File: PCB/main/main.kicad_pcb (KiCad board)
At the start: 2 copper layers, 82.3 x 36.1 mm, 38 parts, among them IC1 LT8316IFE#PBF, Q1 PBHV9050ZF, Q2 IXTA10P50P, Q3 SIHB24N80AE-GE3, T1 Transformer_1P_2S

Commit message: pcb drawing update
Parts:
- C5: moved to B.Cu
- R11: footprint Resistor_SMD:R_0805_2012Metric -> Resistor_SMD:R_1218_3246Metric_Pad1.22x4.75mm_HandSolder; moved to B.Cu
- moved R11 16.4 mm to (101.1, 42.4), turned to 90 degrees
- moved R1 13.5 mm to (87.8, 47.9), turned to 270 degrees
- moved R7 12.2 mm to (92.2, 36.7), turned to 90 degrees
- moved R6 11.3 mm to (87.6, 36.3), turned to 90 degrees
- moved Vin1 10.9 mm to (82.3, 35.3)
- moved R10 10.8 mm to (97.8, 42.8)
- moved D2 10.6 mm to (89.9, 36.2), turned to 270 degrees
- moved REF** 9.63 mm to (79.6, 54.0)
- moved REF** 9.51 mm to (79.5, 27.0)
- moved REF** 8.31 mm to (144.3, 35.3)
- moved C3 8.07 mm to (89.3, 51.8), turned to 270 degrees
- moved C2 7.39 mm to (84.5, 47.9), turned to 90 degrees
- moved C4 7.37 mm to (87.6, 43.6)
- moved D1 7.27 mm to (83.8, 51.2)
- moved R5 6.96 mm to (91.2, 51.7)
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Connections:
- D3 pad 1: Net-(C6-Pad1) -> Net-(D3-Pad1)
- D3 pad 2: Net-(D3-Pad2) -> Net-(C6-Pad1)
- D5 pad 1: Net-(D4-Pad1) -> Net-(C9-Pad2)
- D5 pad 2: Net-(C9-Pad2) -> Net-(D4-Pad1)
- T1 pad 3: Net-(D3-Pad2) -> Net-(D3-Pad1)
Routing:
- net V_FB: track 0.00 -> 62.1 mm
- net GND1: track 0.00 -> 42.0 mm, vias 0 -> 3
- net Net-(IC1-Pad12): track 0.00 -> 26.7 mm
- net Net-(C1-Pad1): track 0.00 -> 17.4 mm
- net Net-(Q1-Pad2): track 0.00 -> 16.0 mm
- net Net-(C9-Pad2): track 0.00 -> 15.0 mm, vias 80 -> 157
- net Net-(C4-Pad1): track 0.00 -> 14.5 mm
- net V_in: track 0.00 -> 14.4 mm, vias 71 -> 96
- net Net-(Q1-Pad3): track 0.00 -> 12.0 mm
- net Net-(IC1-Pad13): track 0.00 -> 11.6 mm
- net Net-(IC1-Pad19): track 0.00 -> 10.9 mm
- net Net-(D4-Pad1): track 0.00 -> 9.95 mm
- net Net-(IC1-Pad18): track 0.00 -> 9.85 mm, vias 0 -> 1
- net Net-(C6-Pad2): track 0.00 -> 8.47 mm
- net Net-(IC1-Pad10): track 0.00 -> 8.47 mm
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- added copper zone on B.Cu, net GND1
- added copper zone on B.Cu, net Net-(C6-Pad1)
- added copper zone on F.Cu, net Net-(C6-Pad1)
- added copper zone on B.Cu, net Net-(C6-Pad2)
- added copper zone on F.Cu, net Net-(C6-Pad2)
- added copper zone on B.Cu, net Net-(C9-Pad2)
- added copper zone on F.Cu, net Net-(C9-Pad2)
- added copper zone on F.Cu, net Net-(D3-Pad1)
- added copper zone on B.Cu, net Net-(D3-Pad2)
- added copper zone on B.Cu, net Net-(IC1-Pad18)
- added copper zone on F.Cu, net Net-(Q1-Pad3)
- added copper zone on B.Cu, net V_in
- added copper zone on F.Cu, net V_in
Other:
- board size 82.3 x 36.1 mm -> 71.2 x 36.8 mm
- net class T_1.5 added: clearance 0.2, trace_width 1.5, via_dia 1, via_drill 0.6

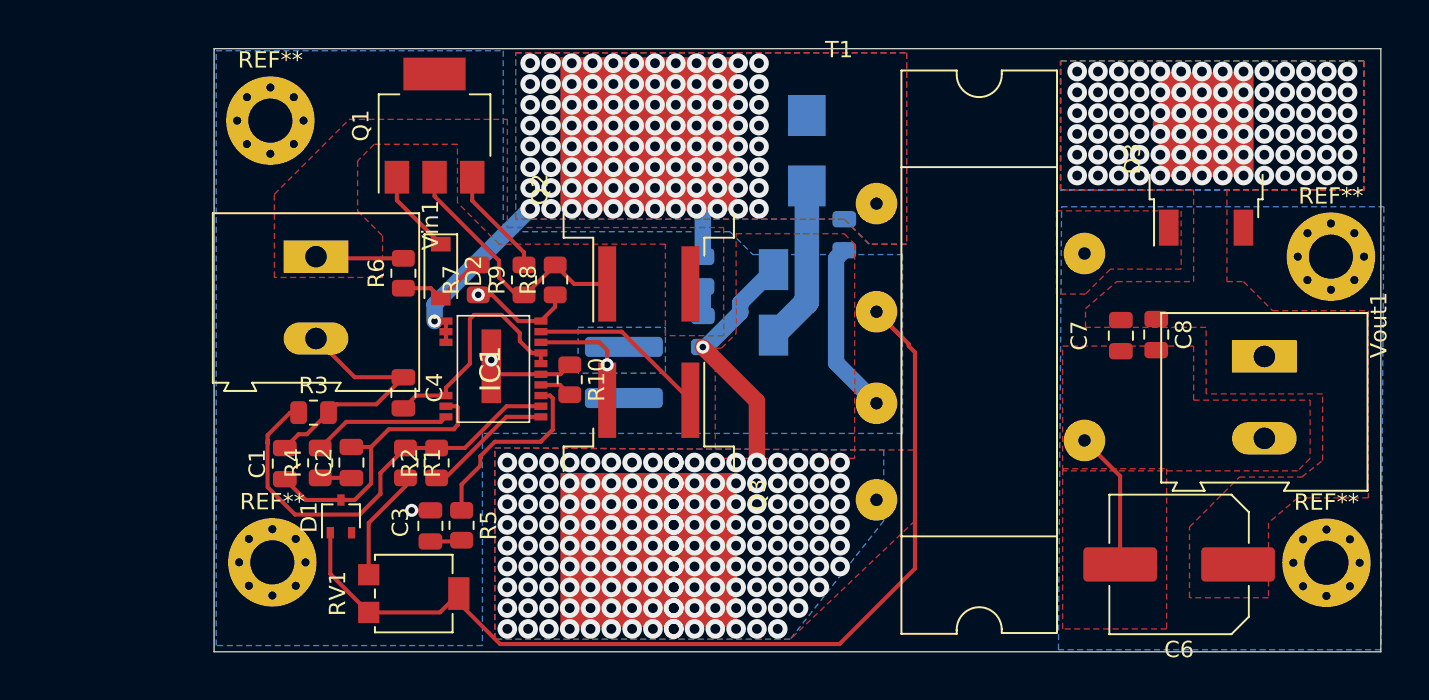
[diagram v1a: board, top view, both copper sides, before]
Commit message: PCB updated with new mosfet&diode
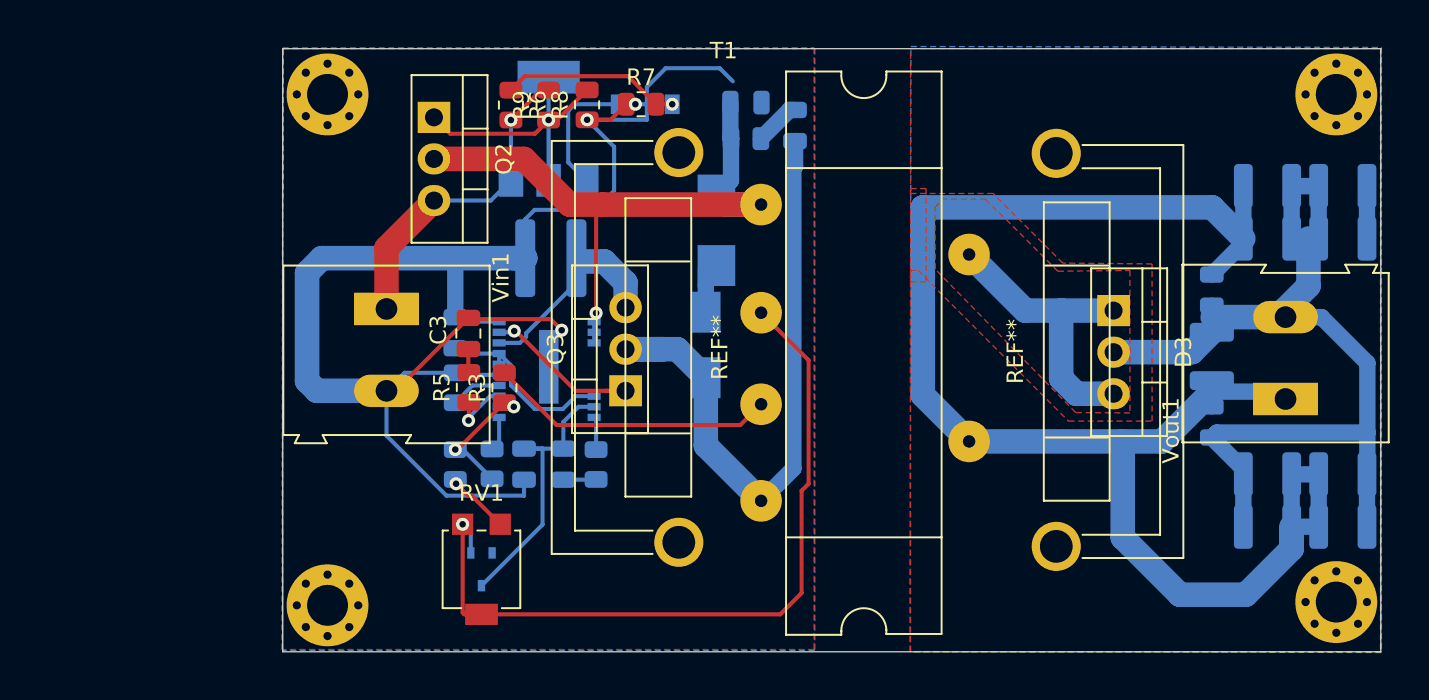
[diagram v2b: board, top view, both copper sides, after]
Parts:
- removed the REF** at (144.0, 54.0)
- removed the REF** at (79.6, 54.0)
- removed the REF** at (79.5, 27.0)
- removed the REF** at (144.3, 35.3)
- added C10: 22uF, Capacitor_SMD:C_1210_3225Metric, B.Cu at (145.0, 34.2)
- added C11: 22uF, Capacitor_SMD:C_1210_3225Metric, B.Cu at (145.0, 48.6)
- added C12: 22uF, Capacitor_SMD:C_1210_3225Metric, B.Cu at (140.4, 34.2)
- added C13: 22uF, Capacitor_SMD:C_1210_3225Metric, B.Cu at (140.4, 48.6)
- added C14: 22uF, Capacitor_SMD:C_1210_3225Metric, B.Cu at (137.0, 41.4)
- added C15: 22uF, Capacitor_SMD:C_1210_3225Metric, B.Cu at (140.4, 31.0)
- added C16: 22uF, Capacitor_SMD:C_1210_3225Metric, B.Cu at (145.0, 51.8)
- added C18: 22uF, Capacitor_SMD:C_1210_3225Metric, B.Cu at (140.4, 51.8)
- added REF**: MountingHole_2.5mm_Pad_Via, MountingHole:MountingHole_2.5mm_Pad_Via, F.Cu at (83.0, 25.4)
- added REF**: MountingHole_2.5mm_Pad_Via, MountingHole:MountingHole_2.5mm_Pad_Via, F.Cu at (83.0, 56.6)
- added REF**: MountingHole_2.5mm_Pad_Via, MountingHole:MountingHole_2.5mm_Pad_Via, F.Cu at (144.6, 56.4)
- added REF**: MountingHole_2.5mm_Pad_Via, MountingHole:MountingHole_2.5mm_Pad_Via, F.Cu at (144.6, 25.4)
- added REF**: Heatsink_Fischer_FK224xx2201_25x8.3mm, Heatsink:Heatsink_Fischer_FK224xx2201_25x8.3mm, F.Cu at (127.5, 53.0)
- added REF**: Heatsink_Fischer_FK224xx2201_25x8.3mm, Heatsink:Heatsink_Fischer_FK224xx2201_25x8.3mm, F.Cu at (104.5, 28.9)
- C1, C2, C4, D1, D2, IC1, Q1, R1, R10, R2, R4: moved to B.Cu
- C6: value 220uF -> 100nf; footprint Capacitor_SMD:C_Elec_8x10.2 -> Capacitor_SMD:C_0805_2012Metric; moved to B.Cu
- C7: value 100nf -> 10nF; moved to B.Cu
- C8: value 10nF -> 22uF; footprint Capacitor_SMD:C_0805_2012Metric -> Capacitor_SMD:C_1210_3225Metric; moved to B.Cu
- D3: value STD12100TR -> TST20U60CW C0G; footprint Package_TO_SOT_SMD:TO-252-2 -> Package_TO_SOT_THT:TO-220-3_Vertical
- D5: value STD12100TR -> SMBJ5386B-TP
- Q2: value IXTA10P50P -> FQP3P50; footprint Package_TO_SOT_SMD:TO-263-2 -> Package_TO_SOT_THT:TO-220-3_Vertical
- Q3: value SIHB24N80AE-GE3 -> FCP190N65S3R0-ND; footprint Package_TO_SOT_SMD:TO-263-2 -> Package_TO_SOT_THT:TO-220-3_Vertical
- moved C6 16.9 mm to (137.0, 37.4), turned to 90 degrees
- moved R4 16.9 mm to (99.4, 48.0)
- moved D2 16.1 mm to (102.4, 26.0), turned to 0 degrees
- moved R7 14.6 mm to (102.2, 26.0), turned to 0 degrees
- moved C1 14.6 mm to (95.0, 48.0), turned to 270 degrees
- moved C8 14.6 mm to (145.0, 31.0), turned to 0 degrees
- moved Q2 13.8 mm to (89.5, 26.8), turned to 270 degrees
- moved C9 13.8 mm to (111.5, 27.3)
- moved C2 12.9 mm to (97.4, 48.0)
- moved R6 12.2 mm to (94.2, 26.1), turned to 270 degrees
- moved C3 12.0 mm to (91.6, 40.0)
- moved R3 11.8 mm to (93.8, 43.3), turned to 90 degrees
- moved R8 10.9 mm to (98.8, 26.0)
- moved D3 10.9 mm to (131.0, 38.6), turned to 270 degrees
- moved R9 10.8 mm to (96.5, 26.1)
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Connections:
- C6 pad 1: Net-(C6-Pad1) -> Net-(C10-Pad1)
- C6 pad 2: Net-(C6-Pad2) -> Net-(C10-Pad2)
- C7 pad 1: Net-(C6-Pad1) -> Net-(C10-Pad1)
- C7 pad 2: Net-(C6-Pad2) -> Net-(C10-Pad2)
- C8 pad 1: Net-(C6-Pad1) -> Net-(C10-Pad1)
- C8 pad 2: Net-(C6-Pad2) -> Net-(C10-Pad2)
- D3 pad 2: Net-(C6-Pad1) -> Net-(C10-Pad1)
- D3 pad 3: (no net) -> Net-(D3-Pad1)
- T1 pad 4: Net-(C6-Pad2) -> Net-(C10-Pad2)
- Vout1 pad 1: Net-(C6-Pad1) -> Net-(C10-Pad2)
- Vout1 pad 2: Net-(C6-Pad2) -> Net-(C10-Pad1)
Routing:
- net Net-(C10-Pad2): track 0.00 -> 98.5 mm
- net GND1: track 42.0 -> 115.7 mm
- net Net-(C10-Pad1): track 0.00 -> 59.8 mm
- net V_in: track 14.4 -> 39.1 mm, vias 96 -> 1
- net Net-(C9-Pad2): track 15.0 -> 39.2 mm, vias 157 -> 0
- net Net-(IC1-Pad12): track 26.7 -> 8.50 mm, vias 0 -> 2
- net Net-(D3-Pad1): track 0.00 -> 18.0 mm
- net V_FB: track 62.1 -> 47.2 mm, vias 0 -> 1
- net Net-(C6-Pad2): track 8.47 -> 0.00 mm
- net Net-(IC1-Pad13): track 11.6 -> 3.74 mm, vias 0 -> 1
- net Net-(Q1-Pad3): track 12.0 -> 19.8 mm, vias 0 -> 1
- net Net-(IC1-Pad10): track 8.47 -> 2.01 mm
- net Net-(IC1-Pad11): track 8.21 -> 2.01 mm
- net Net-(D4-Pad1): track 9.95 -> 4.17 mm
- net Net-(D2-Pad2): track 5.67 -> 10.9 mm, vias 0 -> 1
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- added copper zone on F.Cu, net GND1
- added copper zone on B.Cu, net Net-(C10-Pad2)
- added copper zone on F.Cu, net Net-(C10-Pad2)
- removed copper zone on B.Cu, net Net-(C6-Pad1)
- removed copper zone on F.Cu, net Net-(C6-Pad1)
- removed copper zone on B.Cu, net Net-(C6-Pad2)
- removed copper zone on F.Cu, net Net-(C6-Pad2)
- removed copper zone on B.Cu, net Net-(C9-Pad2)
- removed copper zone on F.Cu, net Net-(C9-Pad2)
- removed copper zone on B.Cu, net Net-(D3-Pad2)
- removed copper zone on B.Cu, net Net-(IC1-Pad18)
- removed copper zone on F.Cu, net Net-(Q1-Pad3)
- removed copper zone on B.Cu, net V_in
- removed copper zone on F.Cu, net V_in
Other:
- board size 71.2 x 36.8 mm -> 67.1 x 36.8 mm

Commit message: script and pcb updated
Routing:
- net Net-(C10-Pad1): track 59.8 -> 71.2 mm
- added copper zone on B.Cu, net Net-(D3-Pad1)
